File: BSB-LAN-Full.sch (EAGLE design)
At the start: 118 parts, among them IC1 LAN8710A-EZC, IC2 TPS2375D, IC3 TX4138, IC4 SY8089AAAC, IC5 ESP32-WROOM-32E, IC6 CH340X, Q1 BC847, Q2 BC857, Q3 BC847, Q4 WPM2015-3/TR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

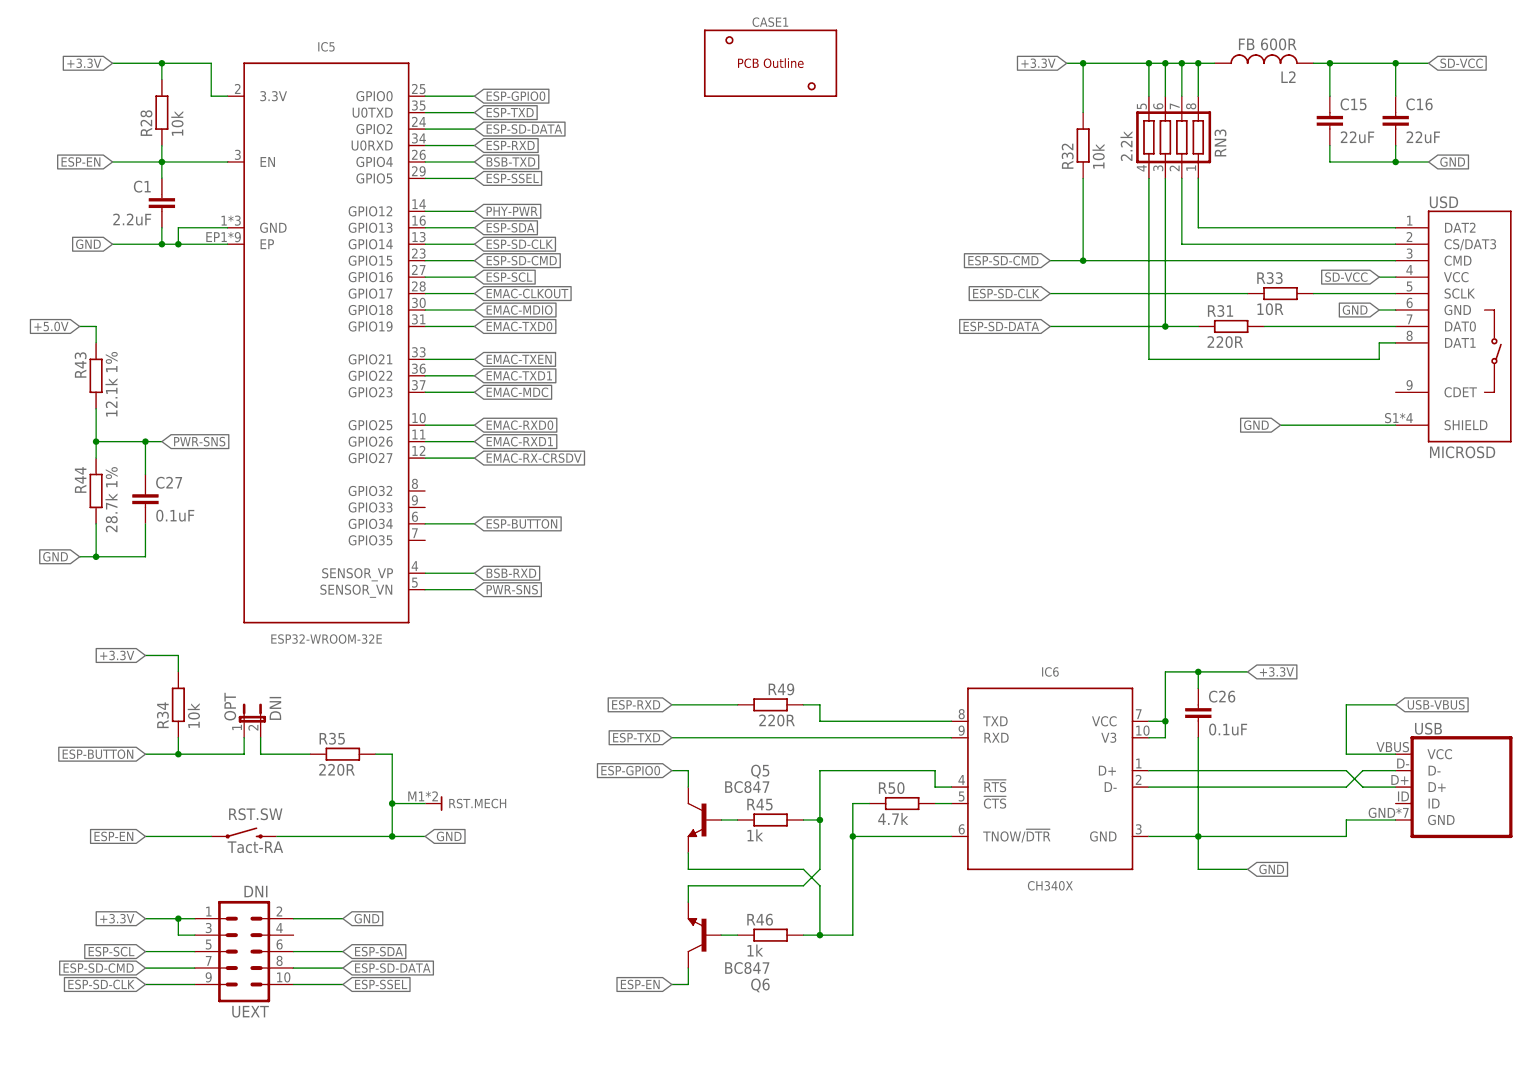
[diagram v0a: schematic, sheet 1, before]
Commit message: Route LAN8710A connections on full PCB
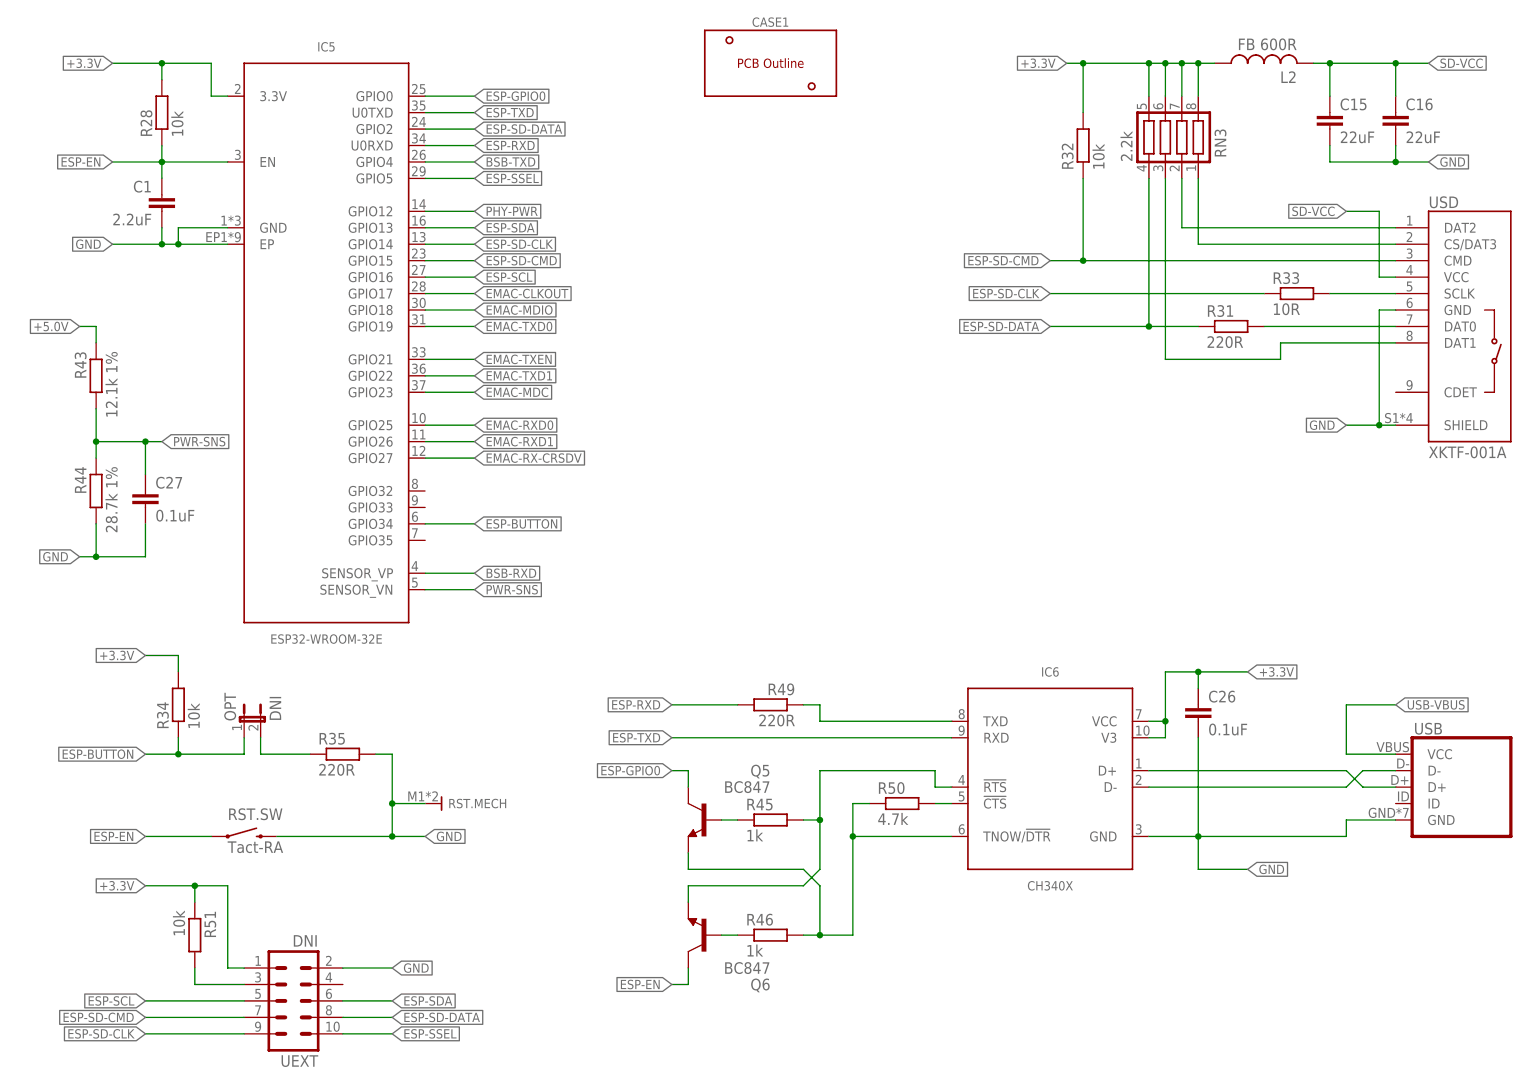
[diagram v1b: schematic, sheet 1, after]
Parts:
- added R51: 10k, BSB-LAN:R-EU_R0402
- USD: value MICROSD -> XKTF-001A
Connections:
- new net UEXT-TX: R51.2, UEXT.3
- net +3.3V: now also R51.1; no longer UEXT.3
- net EMAC-MDIO: now also RN2.4; no longer RN2.3
- net EMAC-RX-CRSDV: now also RN2.3; no longer RN2.4
- net EMAC-RXD0: now also RN2.2; no longer RN2.1
- net EMAC-RXD1: now also RN2.1; no longer RN2.2
- net ESP-SD-DATA: now also RN3.4; no longer RN3.3
- net ETH-PHYAD1: now also RN1.1; no longer RN1.3
- net ETH-RD_N: now also R18.1; no longer R19.1
- net ETH-RD_P: now also R19.2; no longer R18.2
- net ETH-RMIISEL: now also RN1.3; no longer RN1.1
- net ETH-VDDA: now also R18.2, R19.1; no longer R18.1, R19.2
- net ETH-VDDIO: now also RN1.6; no longer RN1.8
- net GND: now also RN1.8; no longer RN1.6
- net SD-DAT1: now also RN3.3; no longer RN3.4
- net SD-DAT2: now also RN3.2; no longer RN3.1
- net SD-DAT3: now also RN3.1; no longer RN3.2
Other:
- moved on the sheet: R18, R19, R33, UEXT

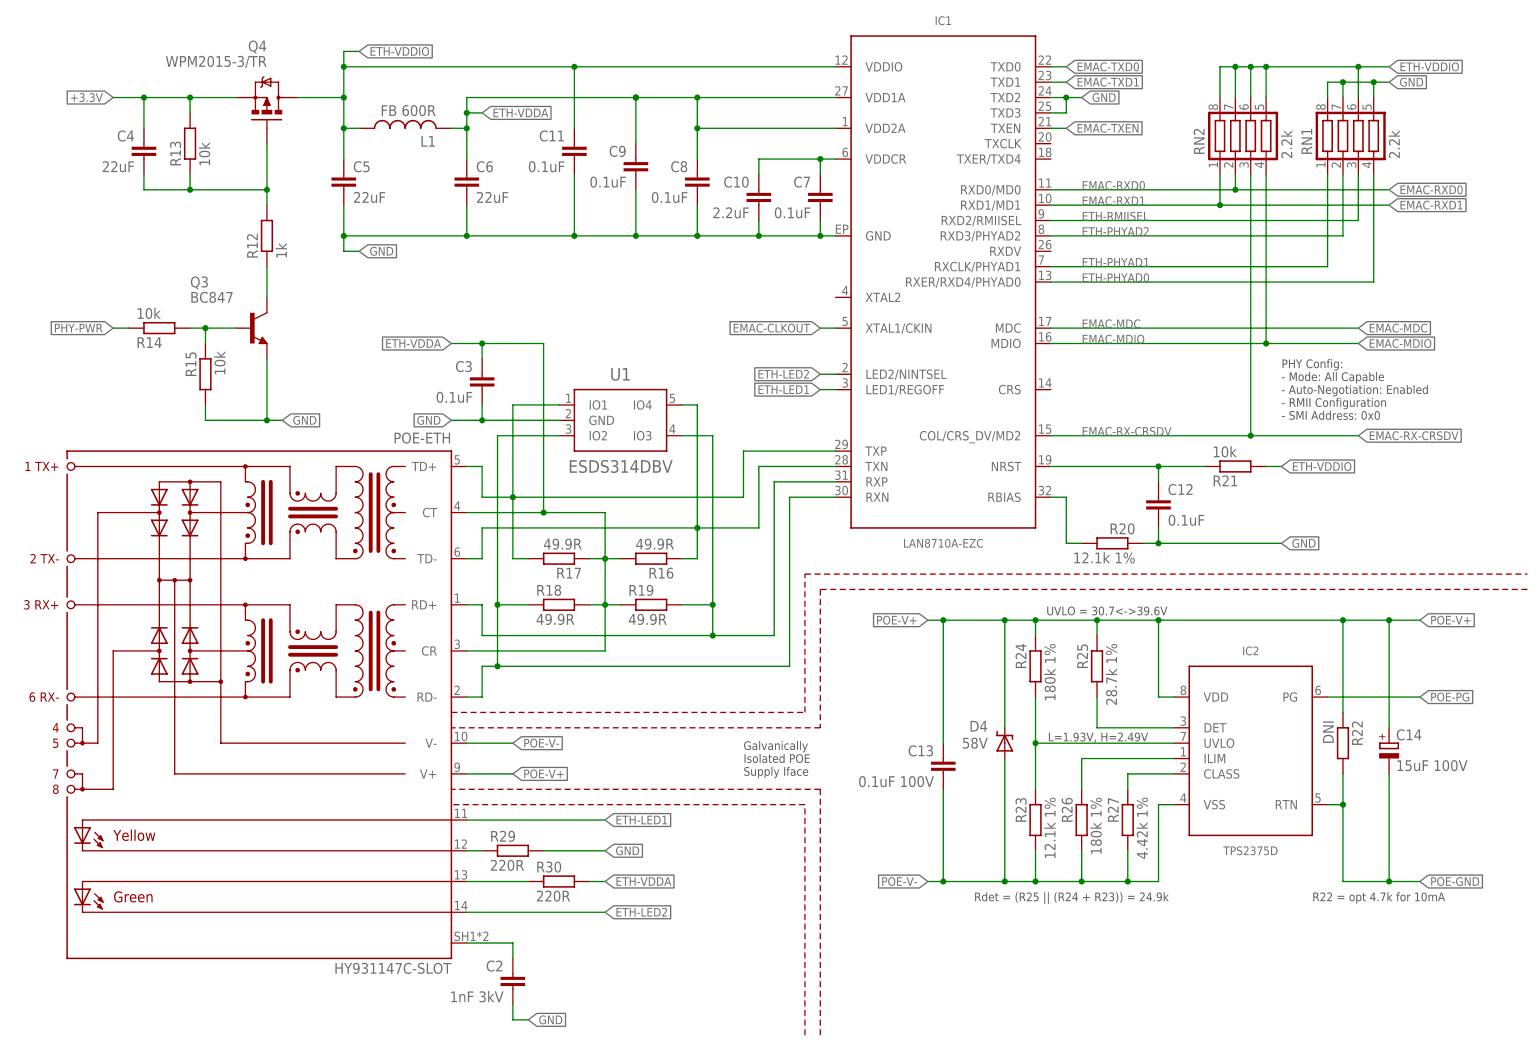
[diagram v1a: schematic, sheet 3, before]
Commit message: Finish Routing Full Board
Route the remaining BSB components, and also fix arrangement of parts on rear of the board which were encroaching the DIN frame keep-out.
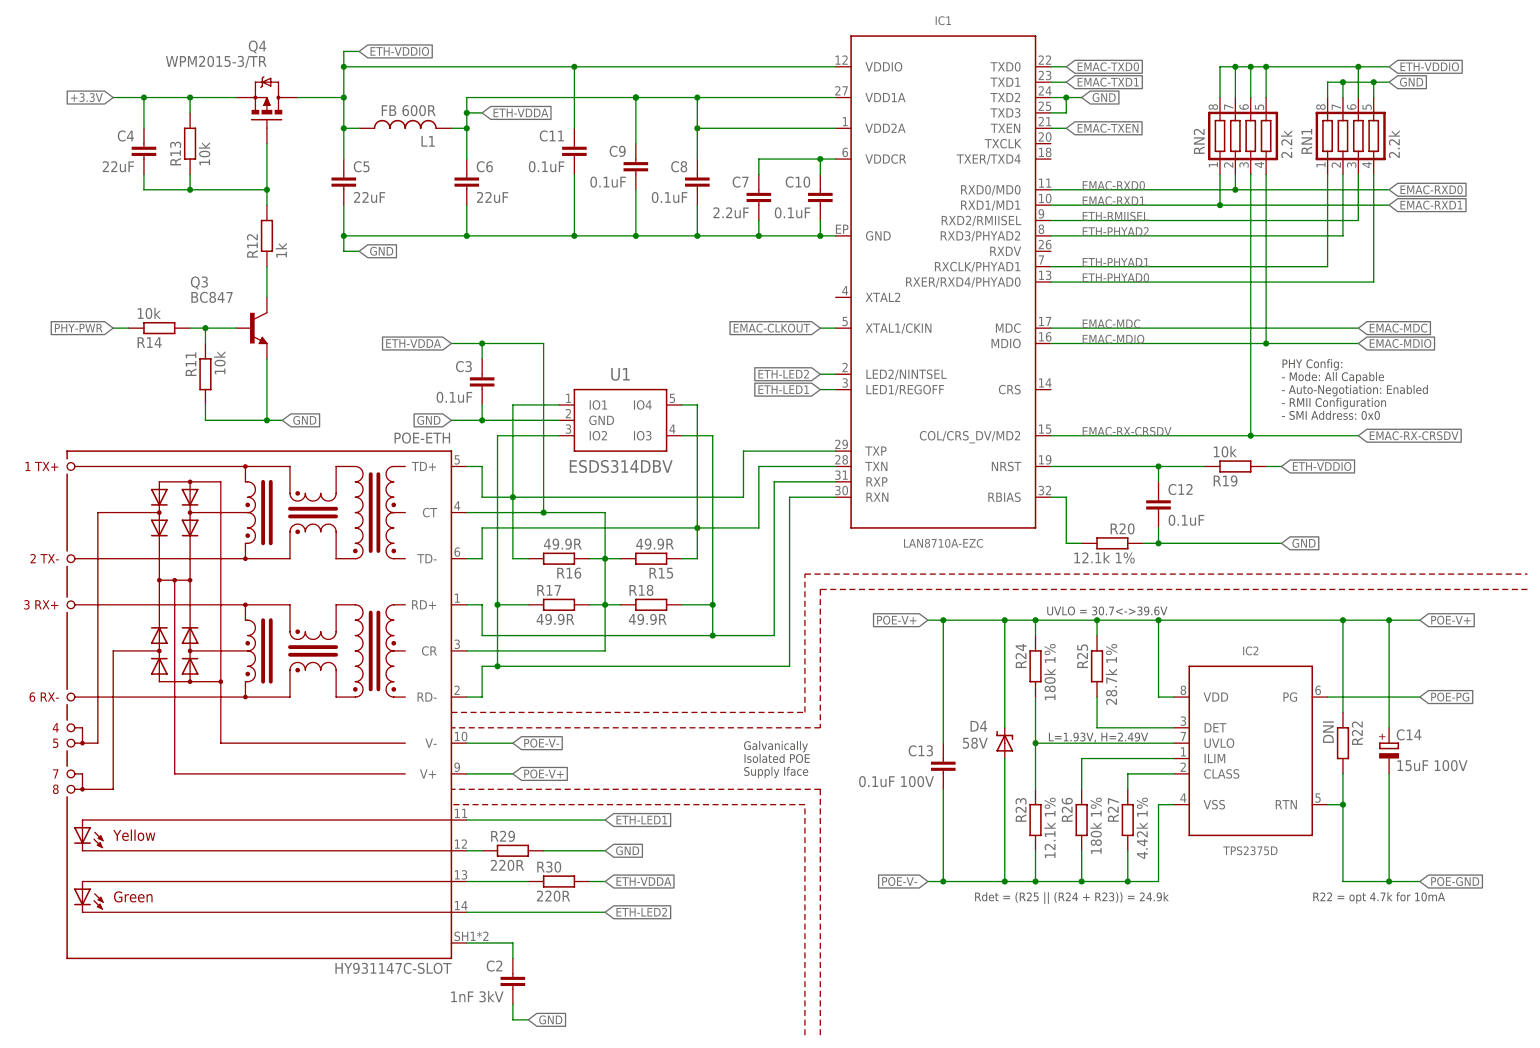
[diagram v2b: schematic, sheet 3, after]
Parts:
- C10: value 2.2uF -> 0.1uF; device BSB-LAN:C-EUC0603 -> BSB-LAN:C-EUC0402
- C7: value 0.1uF -> 2.2uF; device BSB-LAN:C-EUC0402 -> BSB-LAN:C-EUC0603
- R10: value 0.03R 1% -> 10R; device BSB-LAN:R-EU_R1206 -> BSB-LAN:R-EU_R0603
- R11: value 4.7k -> 10k
- R15: value 10k -> 49.9R; device BSB-LAN:R-EU_R0402 -> BSB-LAN:R-EU_R0402L
- R19: value 49.9R -> 10k; device BSB-LAN:R-EU_R0402L -> BSB-LAN:R-EU_R0402
- R21: value 10k -> 0.03R 1%; device BSB-LAN:R-EU_R0402 -> BSB-LAN:R-EU_R1206
- R8: value 10R -> 4.7k; device BSB-LAN:R-EU_R0603 -> BSB-LAN:R-EU_R0402
- renumbered IC5 to ESP1
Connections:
- net BSB+: now also R10.2; no longer R8.2
- net BSB-TXD: now also R8.2; no longer R11.2
- net CON-BSB+: now also R10.1; no longer R8.1
- net ETH-PWR-B: now also R11.1; no longer R15.1
- net ETH-RD_N: now also R17.1; no longer R18.1
- net ETH-RD_P: now also R18.2; no longer R19.2
- net ETH-RST: now also R19.1; no longer R21.1
- net ETH-TD_N: now also R15.1; no longer R16.1
- net ETH-TD_P: now also R16.2; no longer R17.2
- net ETH-VDDA: now also R15.2, R16.1, R17.2, R18.1; no longer R16.2, R17.1, R18.2, R19.1
- net ETH-VDDIO: now also R19.2; no longer R21.2
- net GND: now also R11.2, R8.1; no longer R11.1, R15.2
- net POE-DC-ILIM: now also R21.2; no longer R10.2
- net POE-V+: now also R21.1; no longer R10.1
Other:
- moved on the sheet: C10, C7, R15, R16, R17, R18, R19, R8

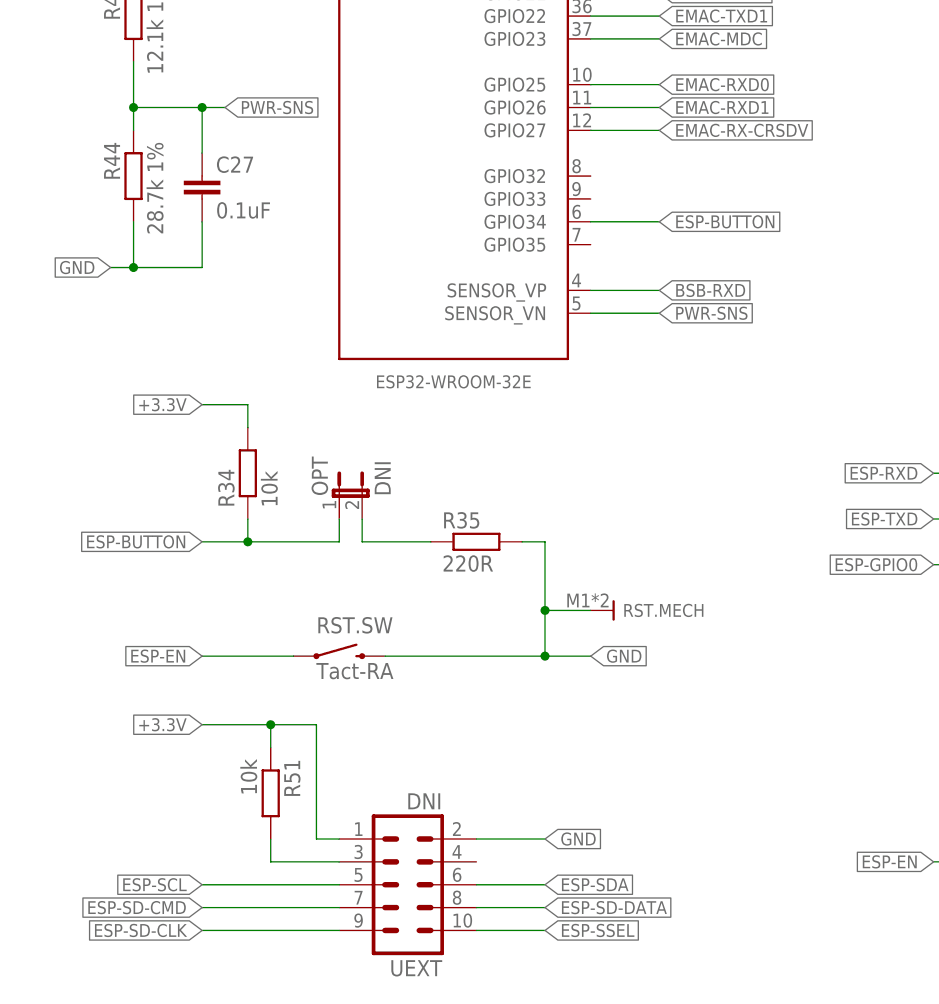
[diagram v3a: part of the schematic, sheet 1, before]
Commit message: Fix USB Position and Pinout UEXT 3/4
1. Move the microUSB port inward so that it doesn't foul the enclosure.
2. Pinout UEXT 3/4 to the spare GPIO pins 32/33. The correct two pins are in use by the BSB interface so they were previously left unconnected on UEXT, but we might as well have other GPIOs connected so we have a fully populated expansion header.
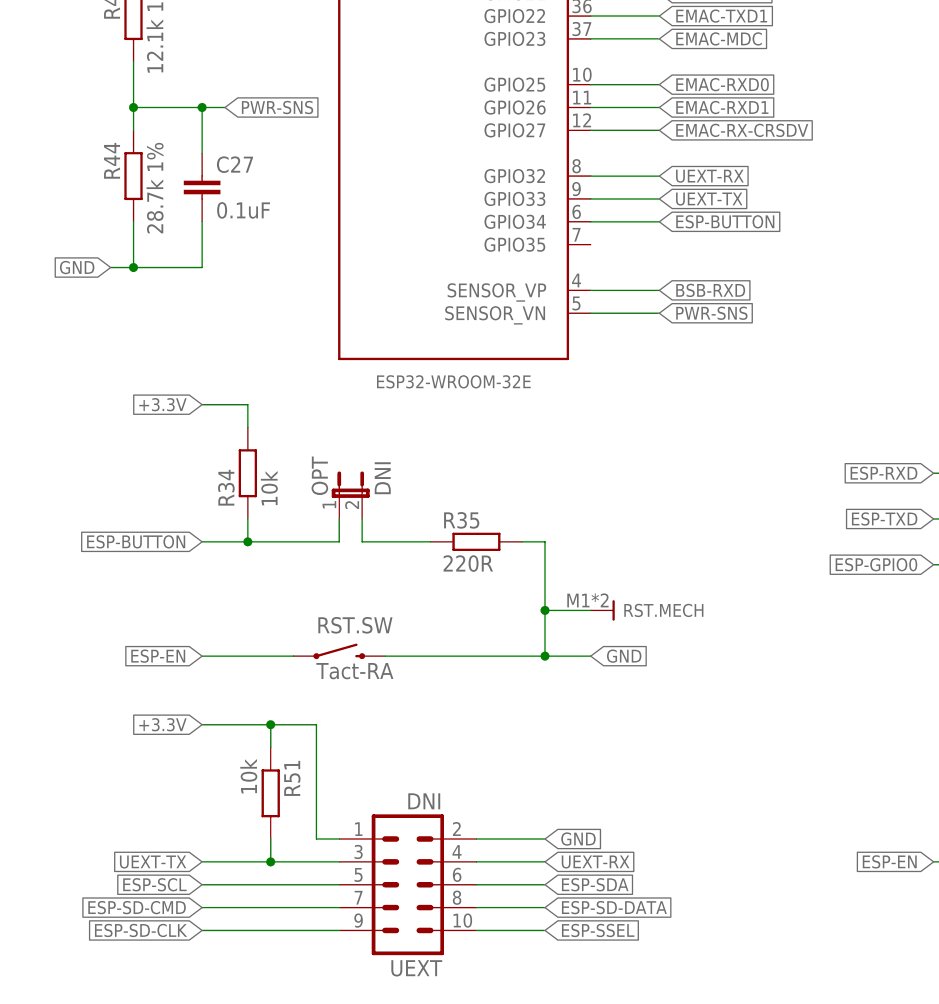
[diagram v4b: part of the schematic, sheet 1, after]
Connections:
- new net UEXT-RX: ESP1.GPIO32, UEXT.4
- net UEXT-TX: now also ESP1.GPIO33
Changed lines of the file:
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@@
 <pinref part="R51" gate="G$1" pin="2"/>
 <wire x1="40.64" y1="22.86" x2="40.64" y2="20.32" width="0.1524" layer="91"/>
+<wire x1="40.64" y1="20.32" x2="33.02" y2="20.32" width="0.1524" layer="91"/>
+<label x="33.02" y="20.32" size="1.4224" layer="95" font="vector" ratio="10" rot="R180" xref="yes"/>
+<junction x="40.64" y="20.32"/>
+</segment>
+<segment>
+<wire x1="76.2" y1="93.98" x2="83.82" y2="93.98" width="0.1524" layer="91"/>
+<label x="83.82" y="93.98" size="1.4224" layer="95" font="vector" ratio="10" xref="yes"/>
+<pinref part="ESP1" gate="G$1" pin="GPIO33"/>
 </segment>
 </net>
+<net name="UEXT-RX" class="0">
+<segment>
+<pinref part="UEXT" gate="G$1" pin="4"/>
+<wire x1="63.5" y1="20.32" x2="71.12" y2="20.32" width="0.1524" layer="91"/>
+<label x="71.12" y="20.32" size="1.4224" layer="95" font="vector" ratio="10" xref="yes"/>
+</segment>
+<segment>
+<wire x1="76.2" y1="96.52" x2="83.82" y2="96.52" width="0.1524" layer="91"/>
+<label x="83.82" y="96.52" size="1.4224" layer="95" font="vector" ratio="10" xref="yes"/>
+<pinref part="ESP1" gate="G$1" pin="GPIO32"/>
+</segment>
+</net>
